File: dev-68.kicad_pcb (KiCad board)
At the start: 2 copper layers, 340 x 147 mm, 212 parts, among them J1 Columns, J2 Rows, J3 RGB LED Matrix A Columns, J4 RGB LED Matrix A Rows, J5 RGB LED Matrix B Columns, J6 RGB LED Matrix B Rows, U1 IS31FL3733-TQ, U2 IS31FL3733-TQ

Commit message: Better placement
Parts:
- removed the J3 at (53.2, -3.25)
- added J3: RPI, Module:Raspberry_Pi_Zero_Socketed_THT_FaceDown_MountingHoles, F.Cu at (155.4, -17.2)
- added J3: RGB LED Matrix A Columns, Connector_PinHeader_2.54mm:PinHeader_2x16_P2.54mm_Vertical, F.Cu at (70.2, 0.75)
- added J7: LED Drivers, Connector_PinHeader_2.54mm:PinHeader_1x04_P2.54mm_Vertical, F.Cu at (145.3, 0.79)
- added J8: Power, Connector_PinHeader_2.54mm:PinHeader_1x04_P2.54mm_Vertical, F.Cu at (223.8, 0.79)
- added REF**: BBB, dev-68:BeagleBone_Black, F.Cu at (208.5, -15.9)
- J4, J6: footprint Connector_PinHeader_2.54mm:PinHeader_1x08_P2.54mm_Vertical -> Connector_PinHeader_2.54mm:PinHeader_2x12_P2.54mm_Vertical
- J5: footprint Connector_PinHeader_2.54mm:PinHeader_1x15_P2.54mm_Vertical -> Connector_PinHeader_2.54mm:PinHeader_2x16_P2.54mm_Vertical
- moved J1 91.9 mm to (196.1, 0.79)
- moved J5 45.9 mm to (261.5, 0.75)
- moved J6 41.5 mm to (254.0, -35.0), turned to 0 degrees
- moved U2 34.0 mm to (269.2, -15.0)
- moved J4 31.5 mm to (63.0, -34.8), turned to 0 degrees
- moved U1 22.3 mm to (80.0, -17.5)
- moved J2 14.7 mm to (165.9, 0.75)
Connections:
- net COL0 renamed COL_0
- net COL1 renamed COL_1
- net COL2 renamed COL_2
- net COL3 renamed COL_3
- net COL4 renamed COL_4
- net COL5 renamed COL_5
- net COL6 renamed COL_6
- net COL7 renamed COL_7
- net ROW0 renamed ROW_0
- net ROW1 renamed ROW_1
- net ROW2 renamed ROW_2
- net ROW3 renamed ROW_3
- net ROW4 renamed ROW_4
- net ROW5 renamed ROW_5
- net ROW6 renamed ROW_6
- net ROW7 renamed ROW_7
- net ROW8 renamed ROW_8
- net ROW9 renamed ROW_9
- J4 pad 2: LED_A_ROW_1 -> A_SW1
- J4 pad 3: LED_A_ROW_2 -> LED_A_ROW_1
- J4 pad 4: LED_A_ROW_3 -> A_SW2
- J4 pad 5: LED_A_ROW_4 -> LED_A_ROW_2
- J4 pad 6: LED_A_ROW_5 -> A_SW3
- J4 pad 7: LED_A_ROW_6 -> LED_A_ROW_3
- J4 pad 8: LED_A_ROW_7 -> A_SW4
- J5 pad 10: LED_B_COL_9 -> B_CS5
- J5 pad 11: LED_B_COL_10 -> LED_B_COL_5
- J5 pad 12: LED_B_COL_11 -> B_CS6
- J5 pad 13: LED_B_COL_12 -> LED_B_COL_6
- J5 pad 14: LED_B_COL_13 -> B_CS7
- J5 pad 15: LED_B_COL_14 -> LED_B_COL_7
- J5 pad 2: LED_B_COL_1 -> B_CS1
- J5 pad 3: LED_B_COL_2 -> LED_B_COL_1
- J5 pad 4: LED_B_COL_3 -> B_CS2
- J5 pad 5: LED_B_COL_4 -> LED_B_COL_2
- J5 pad 6: LED_B_COL_5 -> B_CS3
- J5 pad 7: LED_B_COL_6 -> LED_B_COL_3
- J5 pad 8: LED_B_COL_7 -> B_CS4
- J5 pad 9: LED_B_COL_8 -> LED_B_COL_4
- J6 pad 2: LED_B_ROW_1 -> B_SW1
- J6 pad 3: LED_B_ROW_2 -> LED_B_ROW_1
- J6 pad 4: LED_B_ROW_3 -> B_SW2
- J6 pad 5: LED_B_ROW_4 -> LED_B_ROW_2
- J6 pad 6: LED_B_ROW_5 -> B_SW3
- J6 pad 7: LED_B_ROW_6 -> LED_B_ROW_3
- J6 pad 8: LED_B_ROW_7 -> B_SW4
- U1 pad 10: Net-(U1-Pad10) -> A_SW8
- U1 pad 11: Net-(U1-Pad11) -> A_SW9
- U1 pad 13: Net-(U1-Pad13) -> A_SW10
- U1 pad 14: Net-(U1-Pad14) -> A_SW11
- U1 pad 15: Net-(U1-Pad15) -> A_SW12
- U1 pad 16: Net-(U1-Pad16) -> A_CS1
- U1 pad 17: Net-(U1-Pad17) -> A_CS2
- U1 pad 18: Net-(U1-Pad18) -> A_CS3
- U1 pad 19: Net-(U1-Pad19) -> A_CS4
- U1 pad 2: Net-(U1-Pad2) -> A_SW1
- U1 pad 21: Net-(U1-Pad21) -> A_CS5
- U1 pad 22: Net-(U1-Pad22) -> A_CS6
- U1 pad 23: Net-(U1-Pad23) -> A_CS7
- U1 pad 24: Net-(U1-Pad24) -> A_CS8
- U1 pad 25: Net-(U1-Pad25) -> A_CS9
- U1 pad 26: Net-(U1-Pad26) -> A_CS10
- U1 pad 27: Net-(U1-Pad27) -> A_CS11
- U1 pad 28: Net-(U1-Pad28) -> A_CS12
- U1 pad 3: Net-(U1-Pad3) -> A_SW2
- U1 pad 30: Net-(U1-Pad30) -> A_CS13
- U1 pad 31: Net-(U1-Pad31) -> A_CS14
- U1 pad 32: Net-(U1-Pad32) -> A_CS15
- U1 pad 33: Net-(U1-Pad33) -> A_CS16
- U1 pad 4: Net-(U1-Pad4) -> A_SW3
- U1 pad 41: Net-(U1-Pad41) -> SDA
- U1 pad 42: Net-(U1-Pad42) -> SCL
- U1 pad 45: Net-(U1-Pad45) -> INTB
- U1 pad 46: Net-(U1-Pad46) -> SDB
- U1 pad 6: Net-(U1-Pad6) -> A_SW4
- U1 pad 7: Net-(U1-Pad7) -> A_SW5
- U1 pad 8: Net-(U1-Pad8) -> A_SW6
- U1 pad 9: Net-(U1-Pad9) -> A_SW7
- U2 pad 10: Net-(U2-Pad10) -> B_SW8
- U2 pad 11: Net-(U2-Pad11) -> B_SW9
- U2 pad 13: Net-(U2-Pad13) -> B_SW10
- U2 pad 14: Net-(U2-Pad14) -> B_SW11
- U2 pad 15: Net-(U2-Pad15) -> B_SW12
- U2 pad 16: Net-(U2-Pad16) -> B_CS1
- U2 pad 17: Net-(U2-Pad17) -> B_CS2
- U2 pad 18: Net-(U2-Pad18) -> B_CS3
- U2 pad 19: Net-(U2-Pad19) -> B_CS4
- U2 pad 2: Net-(U2-Pad2) -> B_SW1
- U2 pad 21: Net-(U2-Pad21) -> B_CS5
- U2 pad 22: Net-(U2-Pad22) -> B_CS6
- U2 pad 23: Net-(U2-Pad23) -> B_CS7
- U2 pad 24: Net-(U2-Pad24) -> B_CS8
- U2 pad 25: Net-(U2-Pad25) -> B_CS9
- U2 pad 26: Net-(U2-Pad26) -> B_CS10
- U2 pad 27: Net-(U2-Pad27) -> B_CS11
- U2 pad 28: Net-(U2-Pad28) -> B_CS12
- U2 pad 3: Net-(U2-Pad3) -> B_SW2
- U2 pad 30: Net-(U2-Pad30) -> B_CS13
- U2 pad 31: Net-(U2-Pad31) -> B_CS14
- U2 pad 32: Net-(U2-Pad32) -> B_CS15
- U2 pad 33: Net-(U2-Pad33) -> B_CS16
- U2 pad 4: Net-(U2-Pad4) -> B_SW3
- U2 pad 41: Net-(U2-Pad41) -> SDA
- U2 pad 42: Net-(U2-Pad42) -> SCL
- U2 pad 45: Net-(U2-Pad45) -> INTB
- U2 pad 46: Net-(U2-Pad46) -> SDB
- U2 pad 6: Net-(U2-Pad6) -> B_SW4
- U2 pad 7: Net-(U2-Pad7) -> B_SW5
- U2 pad 8: Net-(U2-Pad8) -> B_SW6
- U2 pad 9: Net-(U2-Pad9) -> B_SW7
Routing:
- net SDA: track 0.00 -> 267.3 mm, vias 0 -> 2
- net SCL: track 0.00 -> 266.6 mm, vias 0 -> 2
- net INTB: track 0.00 -> 266.4 mm, vias 0 -> 2
- net SDB: track 0.00 -> 266.1 mm, vias 0 -> 1
- net LED_A_ROW_7: track 252.3 -> 79.1 mm, vias 6 -> 4
- net LED_A_ROW_6: track 232.7 -> 79.1 mm, vias 6 -> 4
- net ROW_3: track 282.7 -> 141.8 mm, vias 3 -> 1
- net ROW_5: track 256.4 -> 119.1 mm, vias 1 -> 0
- net ROW_4: track 287.7 -> 151.8 mm, vias 3 -> 1
- net LED_B_COL_8: track 228.2 -> 92.8 mm, vias 1 -> 0
- net LED_B_COL_6: track 225.9 -> 91.6 mm, vias 1 -> 0
- net LED_A_ROW_5: track 236.1 -> 102.1 mm, vias 7 -> 5
- net ROW_6: track 239.8 -> 116.0 mm, vias 3 -> 1
- net ROW_1: track 255.2 -> 132.9 mm, vias 3 -> 1
- net ROW_7: track 194.4 -> 76.2 mm, vias 3 -> 1
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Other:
- board size 340 x 147 mm -> 340 x 187.5 mm
- board text added: "/INTB"
- board text added: "/SDB"
- board text added: "0"
- board text added: "1"
- board text added: "2"
- board text added: "3"
- board text added: "4"
- board text added: "5"
- board text added: "6"
- board text added: "7"
- board text added: "8"
- board text added: "9"
- board text added: "DEV-68 XEBOW DEVELOPMENT KEYBOARD REV A0"
- board text added: "GND"
- board text added: "KEY MATRIX"
- board text added: "LED DRIVERS"
- board text added: "POWER"
- board text added: "SCL"
- board text added: "SDA"
- board text added: "VCC"
- board text added: "XEBOW"

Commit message: Update schematic with all required 3733 components
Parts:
- J7: footprint Connector_PinHeader_2.54mm:PinHeader_1x04_P2.54mm_Vertical -> Connector_PinHeader_2.54mm:PinHeader_1x06_P2.54mm_Vertical
- moved U1 210.2 mm to (286.5, -56.4), turned to 270 degrees
- moved J4 162.7 mm to (223.8, -59.5), turned to 90 degrees
- moved J3 150.1 mm to (213.9, -42.9)
- moved J3 120.6 mm to (276.0, -17.2)
- moved REF** 120.6 mm to (329.1, -15.9)
- moved J1 108.0 mm to (304.0, 0.00)
- moved J7 108.0 mm to (253.2, 0.00)
- moved J8 108.0 mm to (331.8, 0.00)
- moved J2 108.0 mm to (273.8, -0.04)
- moved J5 48.7 mm to (213.9, -9.57)
- moved J6 31.4 mm to (223.8, -26.2), turned to 90 degrees
- moved U2 19.1 mm to (286.5, -23.0), turned to 270 degrees
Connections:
- J8 pad 1: Net-(J8-Pad1) -> VCC
- J8 pad 2: Net-(J8-Pad2) -> VCC
- J8 pad 3: Net-(J8-Pad3) -> GND
- J8 pad 4: Net-(J8-Pad4) -> GND
- U1 pad 12: Net-(U1-Pad12) -> GND
- U1 pad 20: Net-(U1-Pad20) -> VCC
- U1 pad 29: Net-(U1-Pad29) -> VCC
- U1 pad 34: Net-(U1-Pad34) -> GND
- U1 pad 35: Net-(U1-Pad35) -> RSET
- U1 pad 37: Net-(U1-Pad37) -> VCC
- U1 pad 38: Net-(U1-Pad38) -> VCC
- U1 pad 40: Net-(U1-Pad40) -> SYNC
- U1 pad 43: Net-(U1-Pad43) -> GND
- U1 pad 44: Net-(U1-Pad44) -> GND
- U1 pad 47: Net-(U1-Pad47) -> IICRST
- U1 pad 48: Net-(U1-Pad48) -> GND
- U1 pad 49: Net-(U1-Pad48) -> GND
- U1 pad 5: Net-(U1-Pad12) -> GND
- U2 pad 12: Net-(U2-Pad12) -> GND
- U2 pad 20: Net-(U2-Pad20) -> VCC
- U2 pad 29: Net-(U2-Pad29) -> VCC
- U2 pad 34: Net-(U2-Pad34) -> GND
- U2 pad 35: Net-(U2-Pad35) -> RSET
- U2 pad 37: Net-(U2-Pad37) -> VCC
- U2 pad 38: Net-(U2-Pad38) -> VCC
- U2 pad 40: Net-(U2-Pad40) -> SYNC
- U2 pad 43: Net-(U2-Pad43) -> VCC
- U2 pad 44: Net-(U2-Pad44) -> GND
- U2 pad 47: Net-(U2-Pad47) -> IICRST
- U2 pad 48: Net-(U2-Pad48) -> GND
- U2 pad 49: Net-(U2-Pad48) -> GND
- U2 pad 5: Net-(U2-Pad12) -> GND
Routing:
- net SDA: track 267.3 -> 99.6 mm, vias 2 -> 3
- net SCL: track 266.6 -> 100.5 mm, vias 2 -> 3
- net INTB: track 266.4 -> 102.2 mm, vias 2 -> 3
- net SDB: track 266.1 -> 103.0 mm, vias 1 -> 3
- net GND: track 0.00 -> 76.5 mm, vias 0 -> 2
- net ROW_2: track 202.9 -> 135.4 mm, vias 2 -> 0
- net LED_B_COL_7: track 155.5 -> 92.9 mm, vias 1 -> 0
- net A_CS1: track 15.1 -> 73.5 mm
- net A_CS2: track 14.2 -> 70.8 mm
- net A_CS3: track 13.4 -> 68.0 mm
- net A_CS4: track 12.5 -> 65.3 mm
- net A_SW1: track 19.7 -> 72.4 mm
- net B_SW1: track 21.8 -> 73.1 mm
- net A_SW2: track 17.8 -> 68.9 mm
- net A_CS5: track 11.9 -> 62.3 mm
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
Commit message: some driver tracing
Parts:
- added C1: 22uF/10V, Capacitor_THT:CP_Radial_D4.0mm_P1.50mm, B.Cu at (267.0, -56.8)
- added C10: 0.1uF, Capacitor_SMD:C_1206_3216Metric_Pad1.42x1.75mm_HandSolder, B.Cu at (271.8, -55.3)
- added C11: 0.1uF, Capacitor_SMD:C_1206_3216Metric_Pad1.42x1.75mm_HandSolder, B.Cu at (271.8, -61.6)
- added C12: 0.1uF, Capacitor_SMD:C_1206_3216Metric_Pad1.42x1.75mm_HandSolder, B.Cu at (273.6, -21.1)
- added C13: 0.1uF, Capacitor_SMD:C_1206_3216Metric_Pad1.42x1.75mm_HandSolder, B.Cu at (273.6, -27.4)
- added C14: 0.1uF, Capacitor_SMD:C_1206_3216Metric_Pad1.42x1.75mm_HandSolder, B.Cu at (273.6, -33.8)
- added C15: 0.47uF, Capacitor_SMD:C_1206_3216Metric_Pad1.42x1.75mm_HandSolder, F.Cu at (369.6, -40.5)
- added C16: 0.47uF, Capacitor_SMD:C_1206_3216Metric_Pad1.42x1.75mm_HandSolder, F.Cu at (375.6, -43.8)
- added C2: 22uF/10V, Capacitor_THT:CP_Radial_D4.0mm_P1.50mm, B.Cu at (267.3, -27.4)
- added C3: 0.47uF, Capacitor_SMD:C_1206_3216Metric_Pad1.42x1.75mm_HandSolder, B.Cu at (275.8, -48.9)
- added C4: 0.47uF, Capacitor_SMD:C_1206_3216Metric_Pad1.42x1.75mm_HandSolder, B.Cu at (275.8, -55.3)
- added C5: 0.47uF, Capacitor_SMD:C_1206_3216Metric_Pad1.42x1.75mm_HandSolder, B.Cu at (275.8, -61.6)
- added C6: 0.47uF, Capacitor_SMD:C_1206_3216Metric_Pad1.42x1.75mm_HandSolder, B.Cu at (277.6, -21.1)
- added C7: 0.47uF, Capacitor_SMD:C_1206_3216Metric_Pad1.42x1.75mm_HandSolder, B.Cu at (277.6, -27.4)
- added C8: 0.47uF, Capacitor_SMD:C_1206_3216Metric_Pad1.42x1.75mm_HandSolder, B.Cu at (277.6, -33.8)
- added C9: 0.1uF, Capacitor_SMD:C_1206_3216Metric_Pad1.42x1.75mm_HandSolder, B.Cu at (271.8, -48.9)
- added R1: 100k, Resistor_SMD:R_1206_3216Metric_Pad1.42x1.75mm_HandSolder, F.Cu at (309.2, -11.8)
- added R2: 1k, Resistor_SMD:R_1206_3216Metric_Pad1.42x1.75mm_HandSolder, F.Cu at (320.8, -21.8)
- added R3: 1k, Resistor_SMD:R_1206_3216Metric_Pad1.42x1.75mm_HandSolder, F.Cu at (312.9, -7.49)
- added R4: 100k, Resistor_SMD:R_1206_3216Metric_Pad1.42x1.75mm_HandSolder, F.Cu at (314.9, -15.2)
- added R5: 100k, Resistor_SMD:R_1206_3216Metric_Pad1.42x1.75mm_HandSolder, F.Cu at (320.8, -18.5)
- added R6: 20k, Resistor_SMD:R_1206_3216Metric_Pad1.42x1.75mm_HandSolder, F.Cu at (369.6, -33.9)
- added R7: 20k, Resistor_SMD:R_1206_3216Metric_Pad1.42x1.75mm_HandSolder, F.Cu at (357.7, -47.1)
- D1, D10, D11, D12, D13, D14, D15, D16, D17, D18, D19, D2, D20, D21, D22, D23, D24, D25, D26, D27, D28, D29, D3, D30, D31, D32, D33, D34, D35, D36, D37, D38, D39, D4, D40, D41, D42, D43, D44, D45, D46, D47, D48, D49, D5, D50, D51, D52, D53, D54, D55, D56, D57, D58, D59, D6, D60, D61, D62, D63, D64, D65, D66, D67, D68, D7, D8, D9: footprint Diode_SMD:D_1206_3216Metric -> Diode_SMD:D_1206_3216Metric_Pad1.42x1.75mm_HandSolder
- J7: footprint Connector_PinHeader_2.54mm:PinHeader_1x06_P2.54mm_Vertical -> Connector_PinHeader_2.54mm:PinHeader_1x05_P2.54mm_Vertical
- J8: footprint Connector_PinHeader_2.54mm:PinHeader_1x04_P2.54mm_Vertical -> Connector_PinHeader_2.54mm:PinHeader_1x05_P2.54mm_Vertical
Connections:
- J7 pad 5: RSET -> IICRST
- U1 pad 35: RSET -> Net-(R6-Pad1)
- U1 pad 39: Net-(U1-Pad39) -> VIO
- U2 pad 35: RSET -> Net-(R7-Pad1)
- U2 pad 39: Net-(U2-Pad39) -> VIO
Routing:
- net VCC: track 0.00 -> 160.6 mm, vias 0 -> 6
- net IICRST: track 0.00 -> 103.9 mm, vias 0 -> 3
- net GND: track 76.5 -> 179.1 mm, vias 2 -> 5
- net B_CS1: track 0.00 -> 73.6 mm
- net B_CS2: track 0.00 -> 70.9 mm
- net B_CS3: track 0.00 -> 68.2 mm
- net B_CS4: track 0.00 -> 65.5 mm
- net B_CS5: track 0.00 -> 63.2 mm
- net B_CS7: track 0.00 -> 61.6 mm
- net B_CS9: track 0.00 -> 61.1 mm
- net B_CS6: track 0.00 -> 60.4 mm
- net B_CS8: track 0.00 -> 58.9 mm
- net B_CS10: track 0.00 -> 57.8 mm
- net B_CS11: track 0.00 -> 55.8 mm
- net B_CS12: track 0.00 -> 53.9 mm
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
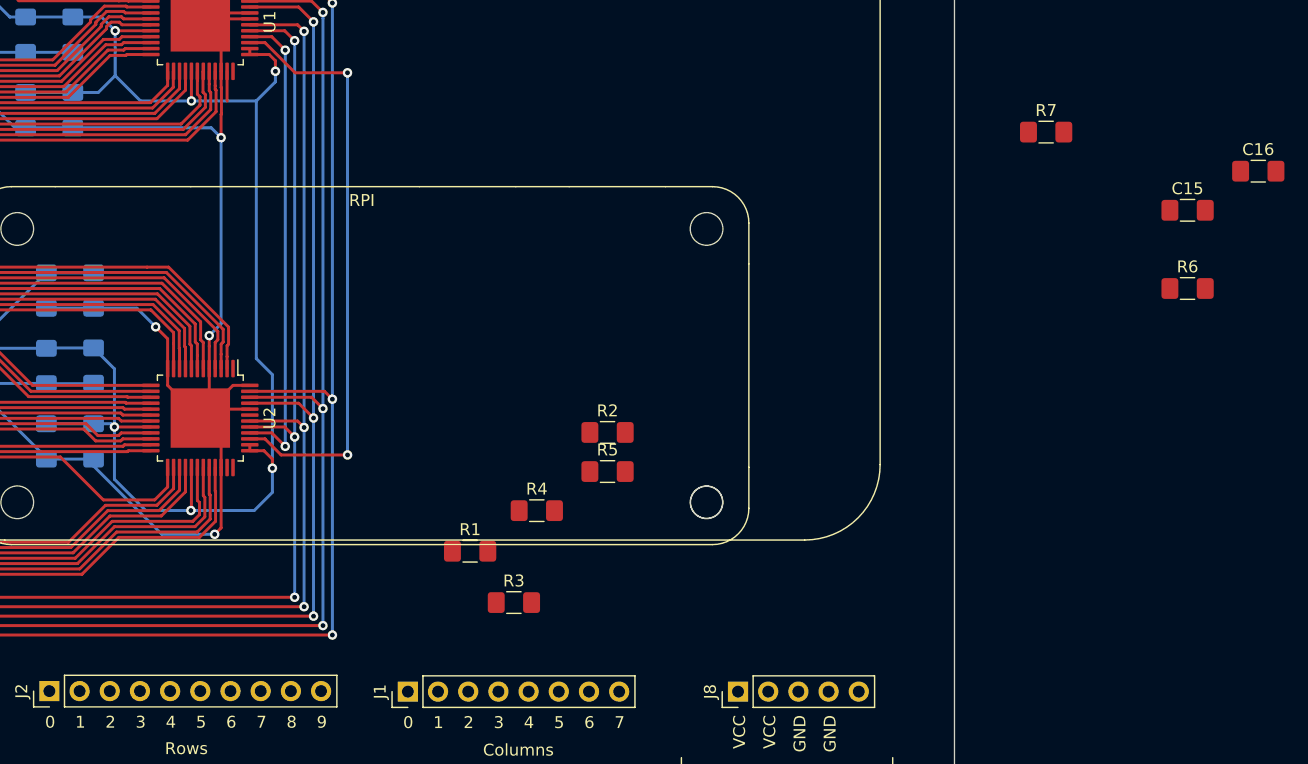
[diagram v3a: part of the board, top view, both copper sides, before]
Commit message: Finished drivver area routing
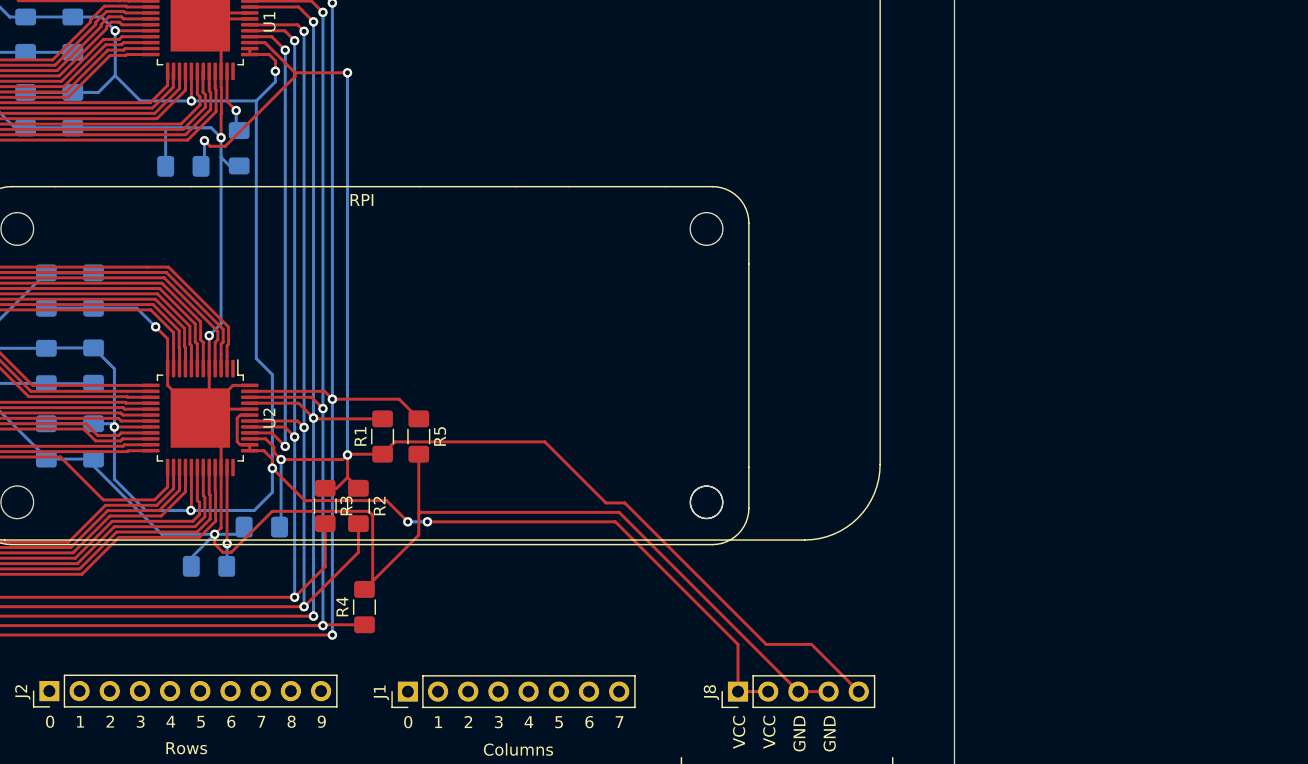
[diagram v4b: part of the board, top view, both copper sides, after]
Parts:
- C15, C16, R6, R7: moved to B.Cu
- moved C16 89.0 mm to (291.7, -13.8), turned to 180 degrees
- moved C15 84.6 mm to (285.1, -44.2), turned to 180 degrees
- moved R6 80.7 mm to (289.8, -45.7), turned to 270 degrees
- moved R7 79.4 mm to (287.3, -10.5), turned to 180 degrees
- moved R2 21.9 mm to (299.8, -15.6), turned to 270 degrees
- moved R3 17.8 mm to (297.1, -15.6), turned to 270 degrees
- moved R4 16.6 mm to (300.4, -7.11), turned to 90 degrees
- moved R5 16.2 mm to (304.9, -21.5), turned to 270 degrees
- moved R1 12.1 mm to (301.9, -21.5), turned to 90 degrees
- renumbered J3 to J9
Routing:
- net GND: track 179.1 -> 266.9 mm
- net VIO: track 50.2 -> 127.0 mm, vias 2 -> 4
- net VCC: track 160.6 -> 216.7 mm, vias 6 -> 8
- net SCL: track 100.5 -> 109.4 mm
- net Net-(R7-Pad1): track 0.00 -> 8.33 mm, vias 0 -> 1
- net IICRST: track 103.9 -> 111.8 mm
- net SDA: track 99.6 -> 106.9 mm
- net INTB: track 102.2 -> 108.0 mm
- net SDB: track 103.0 -> 106.6 mm
- net Net-(R6-Pad1): track 2.51 -> 5.41 mm, vias 0 -> 1

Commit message: Final? revisions
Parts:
- C1, C2: moved to F.Cu
- J3: value RGB LED Matrix A Columns -> Columns
- J4: value RGB LED Matrix A Rows -> Rows
- J5: value RGB LED Matrix B Columns -> Columns
- J6: value RGB LED Matrix B Rows -> Rows
- U1, U2: footprint Package_QFP:TQFP-48-1EP_7x7mm_P0.5mm_EP5x5mm -> Package_QFP:TQFP-48-1EP_7x7mm_P0.5mm_EP5x5mm_ThermalVias
- moved J7 55.6 mm to (308.8, 0.00)
- moved C2 26.3 mm to (286.5, -9.53), turned to 180 degrees
- moved C1 23.9 mm to (285.8, -42.1), turned to 180 degrees
- moved J1 23.8 mm to (280.2, 0.00)
- moved J2 23.8 mm to (250.0, -0.04)
- moved C9 23.5 mm to (295.3, -50.8), turned to 0 degrees
- moved C12 22.8 mm to (296.1, -17.5), turned to 0 degrees
- moved C8 21.9 mm to (285.8, -13.5), turned to 0 degrees
- moved C14 21.0 mm to (285.8, -16.7), turned to 0 degrees
- moved C6 20.0 mm to (296.1, -13.5), turned to 0 degrees
- moved C3 19.6 mm to (295.3, -46.8), turned to 0 degrees
- moved C5 18.1 mm to (285.0, -46.0), turned to 0 degrees
- moved C11 17.5 mm to (285.0, -50.0), turned to 0 degrees
- moved C15 17.1 mm to (295.3, -57.9), turned to 90 degrees
- moved R4 16.7 mm to (305.6, -23.0), turned to 270 degrees
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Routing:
- net LED_A_ROW_0: track 100.2 -> 355.8 mm, vias 5 -> 0
- net ROW_4: track 115.3 -> 353.0 mm, vias 0 -> 1
- net LED_A_COL_14: track 122.0 -> 353.2 mm, vias 0 -> 1
- net LED_A_ROW_1: track 108.0 -> 329.0 mm, vias 5 -> 6
- net LED_A_COL_13: track 122.7 -> 334.3 mm, vias 0 -> 1
- net LED_A_COL_12: track 122.1 -> 330.6 mm, vias 0 -> 1
- net LED_A_ROW_2: track 106.1 -> 312.0 mm, vias 5 -> 6
- net LED_A_ROW_3: track 79.1 -> 264.2 mm
- net LED_B_COL_13: track 122.7 -> 306.8 mm
- net ROW_3: track 141.8 -> 319.5 mm
- net LED_A_ROW_4: track 79.1 -> 250.5 mm
- net ROW_2: track 135.4 -> 291.5 mm, vias 0 -> 1
- net LED_A_ROW_5: track 102.1 -> 257.7 mm
- net LED_A_COL_11: track 152.9 -> 302.1 mm, vias 0 -> 1
- net LED_A_COL_10: track 153.7 -> 302.0 mm, vias 0 -> 1
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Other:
- board text added: "10"
- board text added: "11"
- board text added: "12"
- board text added: "13"
- board text added: "14"
- board text added: "CS1"
- board text added: "CS10"
- board text added: "CS11"
- board text added: "CS12"
- board text added: "CS13"
- board text added: "CS14"
- board text added: "CS15"
- board text added: "CS16"
- board text added: "CS2"
- board text added: "CS3"
- board text added: "CS4"
- board text added: "CS5"
- board text added: "CS6"
- board text added: "CS7"
- board text added: "CS8"
- board text added: "CS9"
- board text added: "DEV-68"
- board text added: "DEV-68 DEVELOPMENT KEYBOARD REV A0"
- board text added: "IICRST"
- board text added: "RGB LED MATRIX A"
- board text added: "RGB LED MATRIX B"
- board text added: "SW1"
- board text added: "SW10"
- board text added: "SW11"
- board text added: "SW12"
- board text added: "SW2"
- board text added: "SW3"
- board text added: "SW4"
- board text added: "SW5"
- board text added: "SW6"
- board text added: "SW7"
- board text added: "SW8"
- board text added: "SW9"
- board text added: "VIO"
- board text removed: "DEV-68 XEBOW DEVELOPMENT KEYBOARD REV A0"
- board text removed: "XEBOW"

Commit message: Cleanup
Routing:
- net GND: track 402.2 -> 386.0 mm
- net VCC: track 214.0 -> 212.1 mm
- net Net-(R7-Pad1): track 4.82 -> 4.26 mm
